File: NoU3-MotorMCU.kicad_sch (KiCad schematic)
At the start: 14 parts, among them U12 PY32F003F16U6TR

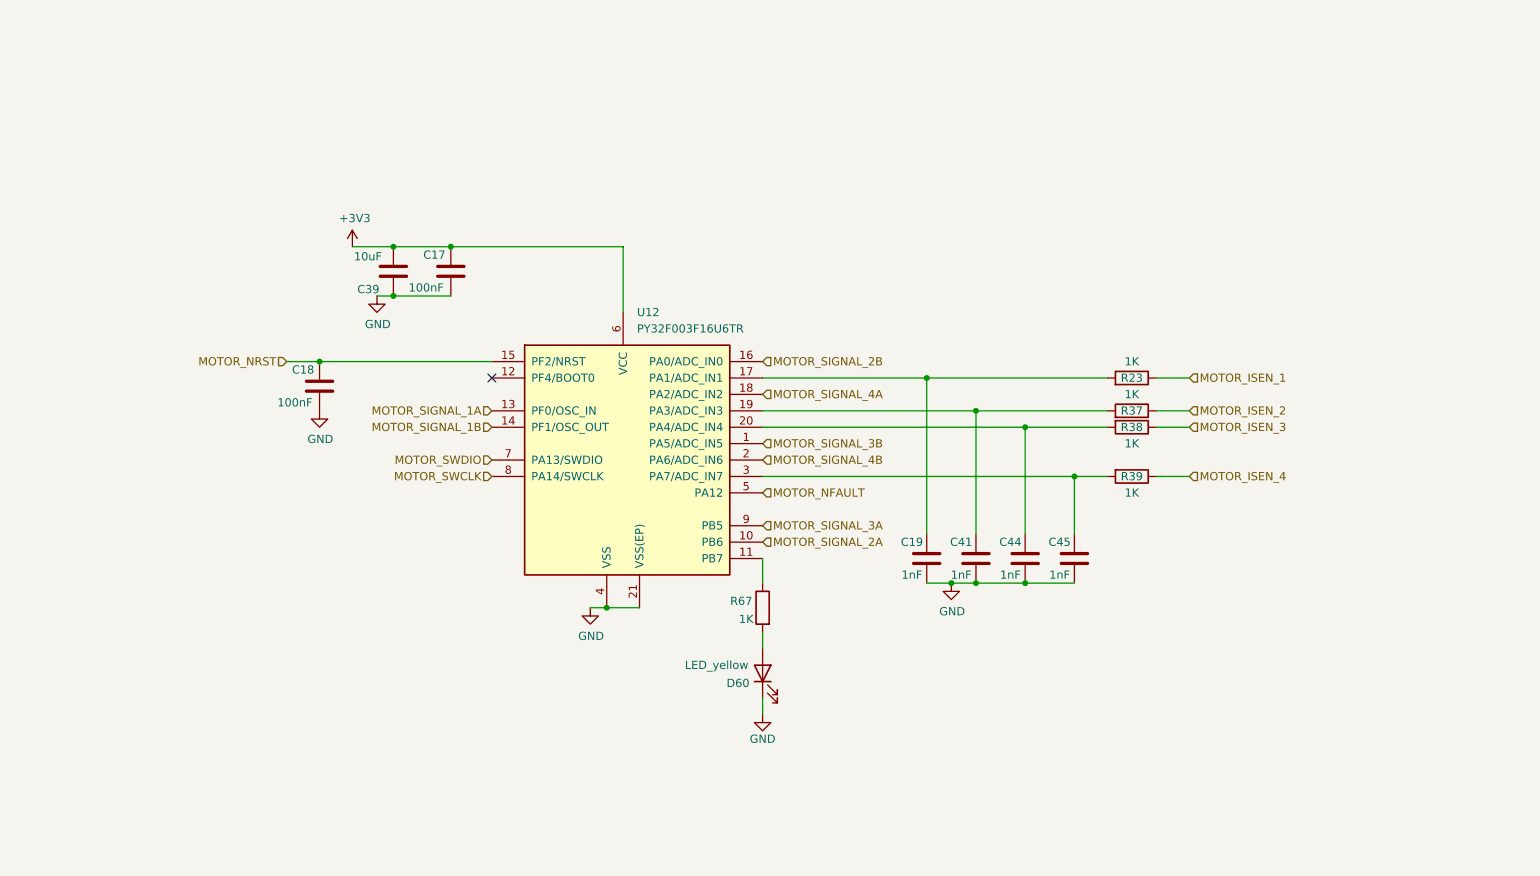
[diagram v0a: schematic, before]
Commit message: PY32F030K28U6TR motor controller chip
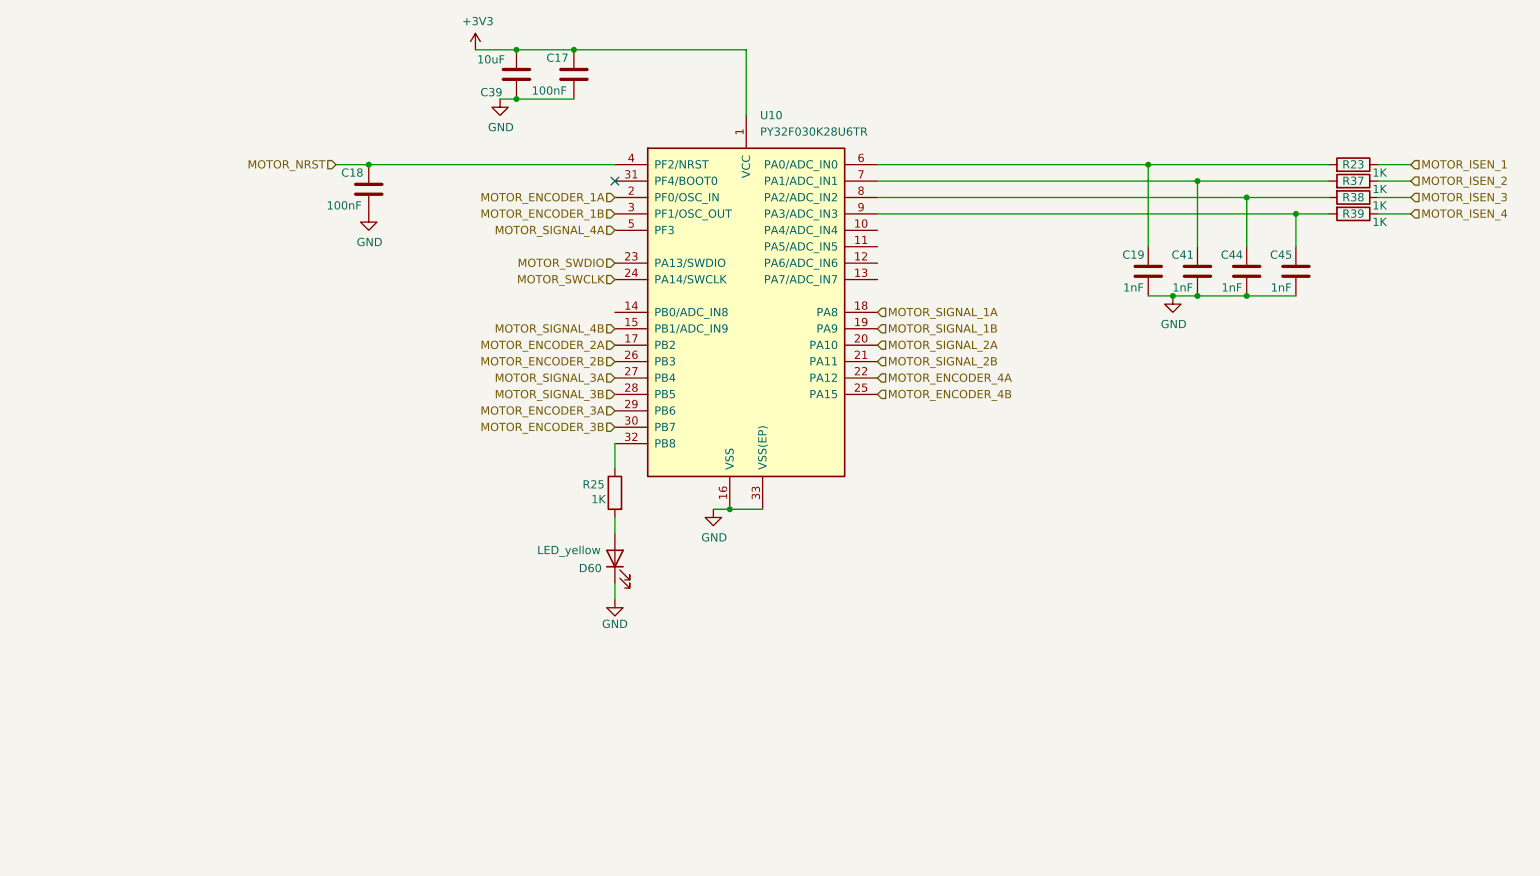
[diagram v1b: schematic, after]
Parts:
- removed R67: 1K, Resistor_SMD:R_0201_0603Metric, symbol Device:R
- removed U12: PY32F003F16U6TR, Package_DFN_QFN:VQFN-20-1EP_3x3mm_P0.4mm_EP1.7x1.7mm, symbol Alfredo_Symbols:PY32F003F16U6TR
- added R25: 1K, Resistor_SMD:R_0402_1005Metric, symbol Device:R
- added U10: PY32F030K28U6TR, Package_DFN_QFN:VQFN-32-1EP_5x5mm_P0.5mm_EP3.5x3.5mm, symbol Alfredo_Symbols:PY32F030K28U6TR
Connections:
- net +3V3: now also U10.1 (VCC)
- net GND: now also U10.16 (VSS), U10.33 (VSS(EP))
- net MOTOR_NRST: now also U10.4 (PF2/NRST)
- net MOTOR_SIGNAL_1A: now also U10.18 (PA8)
- net MOTOR_SIGNAL_1B: now also U10.19 (PA9)
- net MOTOR_SIGNAL_2A: now also U10.20 (PA10)
- net MOTOR_SIGNAL_2B: now also U10.21 (PA11)
- net MOTOR_SIGNAL_3A: now also U10.27 (PB4)
- net MOTOR_SIGNAL_3B: now also U10.28 (PB5)
- net MOTOR_SIGNAL_4A: now also U10.5 (PF3)
- net MOTOR_SIGNAL_4B: now also U10.15 (PB1/ADC_IN9)
- net MOTOR_SWCLK: now also U10.24 (PA14/SWCLK)
- net MOTOR_SWDIO: now also U10.23 (PA13/SWDIO)
- net at C19.1, R23.2: now also U10.6 (PA0/ADC_IN0)
- net at C41.1, R37.2: now also U10.7 (PA1/ADC_IN1)
- net at C44.1, R38.2: now also U10.8 (PA2/ADC_IN2)
- net at C45.1, R39.2: now also U10.9 (PA3/ADC_IN3)
- net at D60.2 (A): now also R25.2
- new net: R25.1, U10.32 (PB8)
- new net MOTOR_ENCODER_1A: U10.2 (PF0/OSC_IN)
- new net MOTOR_ENCODER_1B: U10.3 (PF1/OSC_OUT)
- new net MOTOR_ENCODER_2A: U10.17 (PB2)
- new net MOTOR_ENCODER_2B: U10.26 (PB3)
- new net MOTOR_ENCODER_3A: U10.29 (PB6)
- new net MOTOR_ENCODER_3B: U10.30 (PB7)
- new net MOTOR_ENCODER_4A: U10.22 (PA12)
- new net MOTOR_ENCODER_4B: U10.25 (PA15)
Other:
- moved on the sheet: C17, C18, C19, C39, C41, C44, C45, D60, R23, R37, R38, R39

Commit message: motor driver footprints
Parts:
- removed R23, R37, R38, R39: 1K, Resistor_SMD:R_0402_1005Metric, symbol Device:R
- C19, C41, C44, C45: LCSC (none) -> C1523
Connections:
- net MOTOR_ENCODER_1A: now also U10.30 (PB7); no longer U10.2 (PF0/OSC_IN)
- net MOTOR_ENCODER_1B: now also U10.29 (PB6); no longer U10.3 (PF1/OSC_OUT)
- net MOTOR_ENCODER_2A: now also U10.3 (PF1/OSC_OUT); no longer U10.17 (PB2)
- net MOTOR_ENCODER_2B: now also U10.2 (PF0/OSC_IN); no longer U10.26 (PB3)
- net MOTOR_ENCODER_3A: now also U10.22 (PA12); no longer U10.29 (PB6)
- net MOTOR_ENCODER_3B: now also U10.17 (PB2); no longer U10.30 (PB7)
- net MOTOR_ENCODER_4A: now also U10.26 (PB3); no longer U10.22 (PA12)
- net MOTOR_ISEN_1: now also C19.1, U10.6 (PA0/ADC_IN0)
- net MOTOR_ISEN_2: now also C41.1, U10.7 (PA1/ADC_IN1)
- net MOTOR_ISEN_3: now also C44.1, U10.8 (PA2/ADC_IN2)
- net MOTOR_ISEN_4: now also C45.1, U10.9 (PA3/ADC_IN3)
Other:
- moved on the sheet: C17, C18, C19, C39, C41, C44, C45, D60, R25, U10
